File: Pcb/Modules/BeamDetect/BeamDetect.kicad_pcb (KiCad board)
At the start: 2 copper layers, 50.8 x 20.3 mm, 9 parts, among them J1 JACK_RJ45, U3 TSOP585xx, X1 HOLE, X2 HOLE, X3 HOLE, X4 HOLE

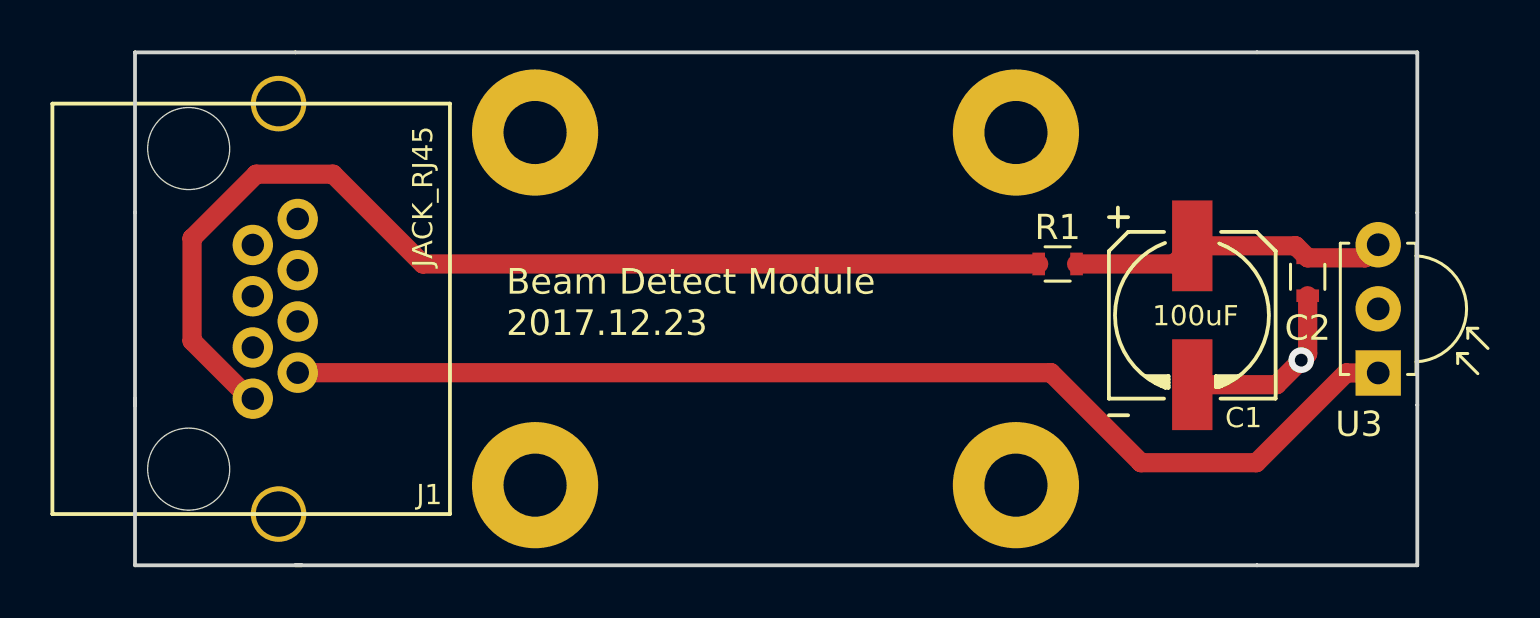
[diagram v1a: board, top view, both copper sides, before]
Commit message: Update module pcbs
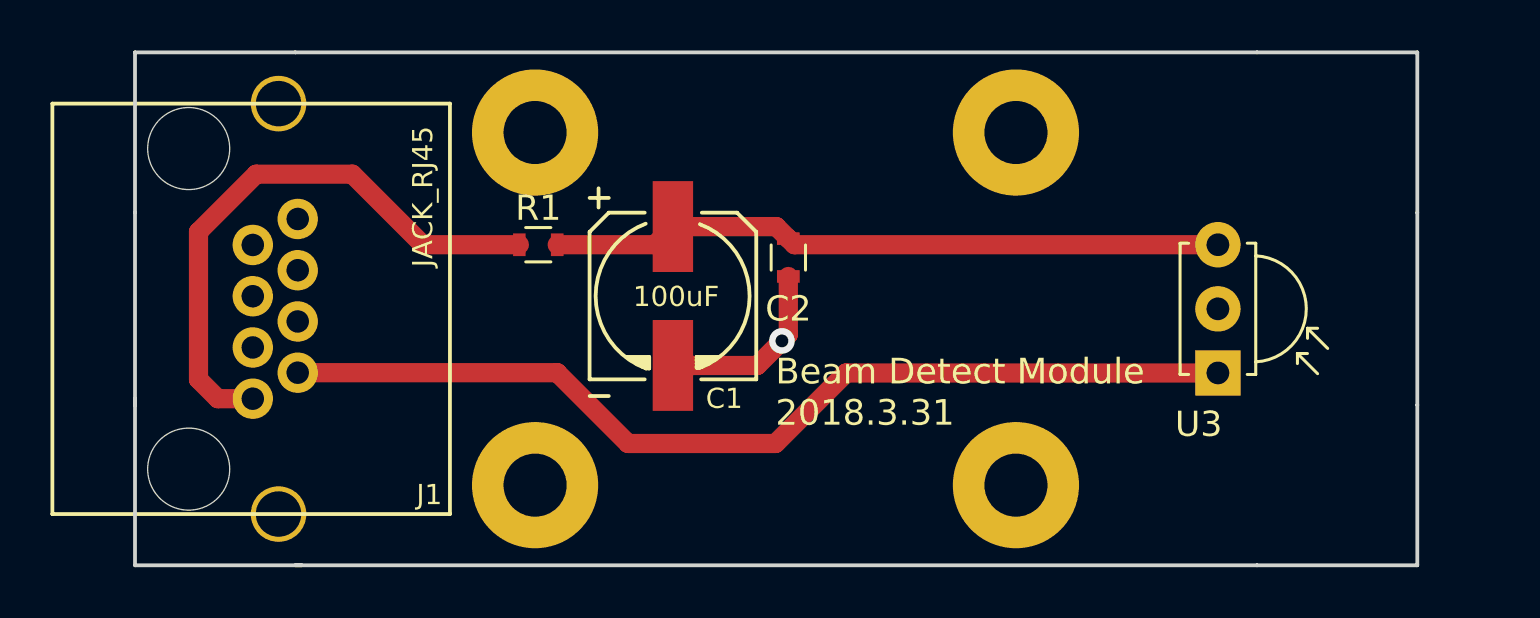
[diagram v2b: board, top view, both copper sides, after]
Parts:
- moved C1 20.6 mm to (56.9, 45.2)
- moved C2 20.6 mm to (61.5, 43.7)
- moved R1 20.6 mm to (51.6, 43.2)
- moved U3 6.35 mm to (78.5, 48.3)
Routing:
- net +3V3: track 43.9 -> 23.6 mm
- net Net-(C1-Pad1): track 12.7 -> 26.8 mm
- net Net-(J1-Pad2): track 46.0 -> 39.0 mm
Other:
- board text added: "Beam Detect Module 2018.3.31"
- board text removed: "Beam Detect Module 2017.12.23"
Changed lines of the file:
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@@
     (thickness 1.6)
     (drawings 13)
-    (tracks 25)
+    (tracks 26)
     (zones 0)
     (modules 9)
@@
   )
   (module Resistors_SMD:R_0603 (layer F.Cu)
-    (at 82.042 44.45 270)
+    (at 61.468 43.688 270)
     (descr "Resistor SMD 0603, reflow soldering, Vishay (see dcrcw.pdf)")
     (tags "resistor 0603")
@@
   )
   (module Opto-Devices:IRReceiver_Vishay_MINICAST-3pin (layer F.Cu)
-    (at 84.836 48.26 90)
+    (at 78.486 48.26 90)
     (descr "IR Receiver Vishay TSOP-xxxx, MINICAST package")
     (tags "IR Receiver Vishay TSOP-xxxx MINICAST")
@@
   )
   (module CA6:c_elec_6.3x5.7 (layer F.Cu)
-    (at 77.47 45.974 90)
+    (at 56.896 45.212 90)
     (descr "SMT capacitor, aluminium electrolytic, 6.3x5.7")
     (fp_text reference C1 (at -4.064 2.032 180) (layer F.SilkS)
@@
   )
   (module Resistors_SMD:R_0603 (layer F.Cu)
-    (at 72.136 43.942)
+    (at 51.562 43.18)
     (descr "Resistor SMD 0603, reflow soldering, Vishay (see dcrcw.pdf)")
     (tags "resistor 0603")
@@
   (gr_line (start 35.5854 41.91) (end 35.5854 49.53) (angle 90) (layer Edge.Cuts) (width 0.15))
   (gr_line (start 86.3854 41.91) (end 86.3854 49.53) (angle 90) (layer Edge.Cuts) (width 0.15))
-  (gr_text "Beam Detect Module\n2017.12.23" (at 50.292 45.466) (layer F.SilkS)
+  (gr_text "Beam Detect Module\n2018.3.31" (at 60.96 49.022) (layer F.SilkS)
     (effects (font (size 1.016 1.016) (thickness 0.2032)) (justify left))
   )
   (gr_line (start 80.0354 55.88) (end 41.9354 55.88) (angle 90) (layer Edge.Cuts) (width 0.15))
   (gr_line (start 41.9354 35.56) (end 80.0354 35.56) (angle 90) (layer Edge.Cuts) (width 0.15))
-  (segment (start 77.47 48.7248) (end 80.8152 48.7248) (width 0.762) (layer F.Cu) (net 1))
-  (segment (start 82.042 47.498) (end 81.788 47.752) (width 0.762) (layer F.Cu) (net 1))
-  (via (at 81.788 47.752) (size 1.016) (drill 0.508) (layers F.Cu B.Cu) (net 1))
-  (segment (start 82.042 47.498) (end 82.042 45.2) (width 0.762) (layer F.Cu) (net 1))
-  (segment (start 80.8152 48.7248) (end 81.788 47.752) (width 0.762) (layer F.Cu) (net 1))
-  (segment (start 42.032 48.25) (end 71.872 48.25) (width 0.762) (layer F.Cu) (net 2))
-  (segment (start 83.566 48.26) (end 84.836 48.26) (width 0.762) (layer F.Cu) (net 2))
-  (segment (start 80.01 51.816) (end 83.566 48.26) (width 0.762) (layer F.Cu) (net 2))
-  (segment (start 75.438 51.816) (end 80.01 51.816) (width 0.762) (layer F.Cu) (net 2))
-  (segment (start 71.872 48.25) (end 75.438 51.816) (width 0.762) (layer F.Cu) (net 2))
-  (segment (start 84.836 48.26) (end 84.582 48.26) (width 0.508) (layer F.Cu) (net 2))
+  (segment (start 56.896 47.9628) (end 60.2412 47.9628) (width 0.762) (layer F.Cu) (net 1))
+  (segment (start 61.468 46.736) (end 61.214 46.99) (width 0.762) (layer F.Cu) (net 1))
+  (via (at 61.214 46.99) (size 1.016) (drill 0.508) (layers F.Cu B.Cu) (net 1))
+  (segment (start 61.468 46.736) (end 61.468 44.438) (width 0.762) (layer F.Cu) (net 1))
+  (segment (start 60.2412 47.9628) (end 61.214 46.99) (width 0.762) (layer F.Cu) (net 1))
+  (segment (start 78.486 48.26) (end 63.754 48.26) (width 0.762) (layer F.Cu) (net 2) (status 10))
+  (segment (start 52.314 48.25) (end 42.032 48.25) (width 0.762) (layer F.Cu) (net 2))
+  (segment (start 55.118 51.054) (end 52.314 48.25) (width 0.762) (layer F.Cu) (net 2))
+  (segment (start 60.96 51.054) (end 55.118 51.054) (width 0.762) (layer F.Cu) (net 2))
+  (segment (start 63.754 48.26) (end 60.96 51.054) (width 0.762) (layer F.Cu) (net 2))
+  (segment (start 78.486 48.26) (end 78.232 48.26) (width 0.508) (layer F.Cu) (net 2) (status 30))
+  (segment (start 38.866 49.28) (end 40.252 49.28) (width 0.762) (layer F.Cu) (net 3))
+  (segment (start 38.1 48.514) (end 38.866 49.28) (width 0.762) (layer F.Cu) (net 3))
+  (segment (start 38.1 42.672) (end 38.1 48.514) (width 0.762) (layer F.Cu) (net 3))
+  (segment (start 40.386 40.386) (end 38.1 42.672) (width 0.762) (layer F.Cu) (net 3))
+  (segment (start 44.196 40.386) (end 40.386 40.386) (width 0.762) (layer F.Cu) (net 3))
+  (segment (start 46.99 43.18) (end 44.196 40.386) (width 0.762) (layer F.Cu) (net 3))
+  (segment (start 50.812 43.18) (end 46.99 43.18) (width 0.762) (layer F.Cu) (net 3))
   (segment (start 40.252 49.28) (end 40.136 49.28) (width 0.762) (layer F.Cu) (net 3))
-  (segment (start 40.136 49.28) (end 37.846 46.99) (width 0.762) (layer F.Cu) (net 3))
-  (segment (start 46.99 43.942) (end 71.386 43.942) (width 0.762) (layer F.Cu) (net 3))
-  (segment (start 43.434 40.386) (end 46.99 43.942) (width 0.762) (layer F.Cu) (net 3))
-  (segment (start 40.386 40.386) (end 43.434 40.386) (width 0.762) (layer F.Cu) (net 3))
-  (segment (start 37.846 42.926) (end 40.386 40.386) (width 0.762) (layer F.Cu) (net 3))
-  (segment (start 37.846 46.99) (end 37.846 42.926) (width 0.762) (layer F.Cu) (net 3))
   (segment (start 40.252 49.28) (end 40.644 49.28) (width 0.762) (layer F.Cu) (net 3))
-  (segment (start 82.042 43.7) (end 84.316 43.7) (width 0.762) (layer F.Cu) (net 4))
-  (segment (start 84.316 43.7) (end 84.836 43.18) (width 0.762) (layer F.Cu) (net 4))
-  (segment (start 77.47 43.2232) (end 81.5652 43.2232) (width 0.762) (layer F.Cu) (net 4))
-  (segment (start 81.5652 43.2232) (end 82.042 43.7) (width 0.762) (layer F.Cu) (net 4))
-  (segment (start 72.886 43.942) (end 76.7512 43.942) (width 0.762) (layer F.Cu) (net 4))
-  (segment (start 76.7512 43.942) (end 77.47 43.2232) (width 0.762) (layer F.Cu) (net 4))
+  (segment (start 78.486 43.18) (end 61.71 43.18) (width 0.762) (layer F.Cu) (net 4) (status 10))
+  (segment (start 61.71 43.18) (end 61.468 42.938) (width 0.762) (layer F.Cu) (net 4))
+  (segment (start 56.896 42.4612) (end 60.9912 42.4612) (width 0.762) (layer F.Cu) (net 4))
+  (segment (start 60.9912 42.4612) (end 61.468 42.938) (width 0.762) (layer F.Cu) (net 4))
+  (segment (start 52.312 43.18) (end 56.1772 43.18) (width 0.762) (layer F.Cu) (net 4))
+  (segment (start 56.1772 43.18) (end 56.896 42.4612) (width 0.762) (layer F.Cu) (net 4))
   (zone (net 1) (net_name GND) (layer B.Cu) (hatch edge 0.508)
     (connect_pads (clearance 0.508))

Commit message: Update pcbs
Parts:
- moved U3 5.71 mm to (84.2, 48.3)
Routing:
- net Net-(C1-Pad1): track 26.8 -> 32.5 mm
- net Net-(J1-Pad2): track 39.0 -> 44.7 mm
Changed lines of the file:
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@@
     (links 10)
     (no_connects 0)
-    (area 31.983069 34.206 89.500001 57.334)
+    (area 31.983069 34.206 86.460401 57.334)
     (thickness 1.6)
     (drawings 13)
@@
   )
   (module Opto-Devices:IRReceiver_Vishay_MINICAST-3pin (layer F.Cu)
-    (at 78.486 48.26 90)
+    (at 84.201 48.26 90)
     (descr "IR Receiver Vishay TSOP-xxxx, MINICAST package")
     (tags "IR Receiver Vishay TSOP-xxxx MINICAST")
@@
   (gr_line (start 35.5854 41.91) (end 35.5854 49.53) (angle 90) (layer Edge.Cuts) (width 0.15))
   (gr_line (start 86.3854 41.91) (end 86.3854 49.53) (angle 90) (layer Edge.Cuts) (width 0.15))
-  (gr_text "Beam Detect Module\n2018.3.31" (at 60.96 49.022) (layer F.SilkS)
+  (gr_text "Beam Detect Module\n2018.3.31" (at 64.77 46.101) (layer F.SilkS)
     (effects (font (size 1.016 1.016) (thickness 0.2032)) (justify left))
   )
   (gr_line (start 80.0354 55.88) (end 41.9354 55.88) (angle 90) (layer Edge.Cuts) (width 0.15))
   (gr_line (start 41.9354 35.56) (end 80.0354 35.56) (angle 90) (layer Edge.Cuts) (width 0.15))
-  (segment (start 56.896 47.9628) (end 60.2412 47.9628) (width 0.762) (layer F.Cu) (net 1))
+  (segment (start 56.896 47.9628) (end 60.2412 47.9628) (width 0.762) (layer F.Cu) (net 1) (status 10))
   (segment (start 61.468 46.736) (end 61.214 46.99) (width 0.762) (layer F.Cu) (net 1))
   (via (at 61.214 46.99) (size 1.016) (drill 0.508) (layers F.Cu B.Cu) (net 1))
-  (segment (start 61.468 46.736) (end 61.468 44.438) (width 0.762) (layer F.Cu) (net 1))
+  (segment (start 61.468 46.736) (end 61.468 44.438) (width 0.762) (layer F.Cu) (net 1) (status 20))
   (segment (start 60.2412 47.9628) (end 61.214 46.99) (width 0.762) (layer F.Cu) (net 1))
-  (segment (start 78.486 48.26) (end 63.754 48.26) (width 0.762) (layer F.Cu) (net 2) (status 10))
-  (segment (start 52.314 48.25) (end 42.032 48.25) (width 0.762) (layer F.Cu) (net 2))
+  (segment (start 84.201 48.26) (end 63.754 48.26) (width 0.762) (layer F.Cu) (net 2) (status 10))
+  (segment (start 52.314 48.25) (end 42.032 48.25) (width 0.762) (layer F.Cu) (net 2) (status 20))
   (segment (start 55.118 51.054) (end 52.314 48.25) (width 0.762) (layer F.Cu) (net 2))
   (segment (start 60.96 51.054) (end 55.118 51.054) (width 0.762) (layer F.Cu) (net 2))
   (segment (start 63.754 48.26) (end 60.96 51.054) (width 0.762) (layer F.Cu) (net 2))
-  (segment (start 78.486 48.26) (end 78.232 48.26) (width 0.508) (layer F.Cu) (net 2) (status 30))
-  (segment (start 38.866 49.28) (end 40.252 49.28) (width 0.762) (layer F.Cu) (net 3))
+  (segment (start 84.201 48.26) (end 83.947 48.26) (width 0.508) (layer F.Cu) (net 2) (status 30))
+  (segment (start 38.866 49.28) (end 40.252 49.28) (width 0.762) (layer F.Cu) (net 3) (status 20))
   (segment (start 38.1 48.514) (end 38.866 49.28) (width 0.762) (layer F.Cu) (net 3))
   (segment (start 38.1 42.672) (end 38.1 48.514) (width 0.762) (layer F.Cu) (net 3))
@@
   (segment (start 44.196 40.386) (end 40.386 40.386) (width 0.762) (layer F.Cu) (net 3))
   (segment (start 46.99 43.18) (end 44.196 40.386) (width 0.762) (layer F.Cu) (net 3))
-  (segment (start 50.812 43.18) (end 46.99 43.18) (width 0.762) (layer F.Cu) (net 3))
-  (segment (start 40.252 49.28) (end 40.136 49.28) (width 0.762) (layer F.Cu) (net 3))
-  (segment (start 40.252 49.28) (end 40.644 49.28) (width 0.762) (layer F.Cu) (net 3))
-  (segment (start 78.486 43.18) (end 61.71 43.18) (width 0.762) (layer F.Cu) (net 4) (status 10))
-  (segment (start 61.71 43.18) (end 61.468 42.938) (width 0.762) (layer F.Cu) (net 4))
-  (segment (start 56.896 42.4612) (end 60.9912 42.4612) (width 0.762) (layer F.Cu) (net 4))
-  (segment (start 60.9912 42.4612) (end 61.468 42.938) (width 0.762) (layer F.Cu) (net 4))
-  (segment (start 52.312 43.18) (end 56.1772 43.18) (width 0.762) (layer F.Cu) (net 4))
-  (segment (start 56.1772 43.18) (end 56.896 42.4612) (width 0.762) (layer F.Cu) (net 4))
+  (segment (start 50.812 43.18) (end 46.99 43.18) (width 0.762) (layer F.Cu) (net 3) (status 10))
+  (segment (start 40.252 49.28) (end 40.136 49.28) (width 0.762) (layer F.Cu) (net 3) (status 30))
+  (segment (start 40.252 49.28) (end 40.644 49.28) (width 0.762) (layer F.Cu) (net 3) (status 30))
+  (segment (start 84.201 43.18) (end 61.71 43.18) (width 0.762) (layer F.Cu) (net 4) (status 30))
+  (segment (start 61.71 43.18) (end 61.468 42.938) (width 0.762) (layer F.Cu) (net 4) (status 30))
+  (segment (start 56.896 42.4612) (end 60.9912 42.4612) (width 0.762) (layer F.Cu) (net 4) (status 10))
+  (segment (start 60.9912 42.4612) (end 61.468 42.938) (width 0.762) (layer F.Cu) (net 4) (status 20))
+  (segment (start 52.312 43.18) (end 56.1772 43.18) (width 0.762) (layer F.Cu) (net 4) (status 30))
+  (segment (start 56.1772 43.18) (end 56.896 42.4612) (width 0.762) (layer F.Cu) (net 4) (status 30))
   (zone (net 1) (net_name GND) (layer B.Cu) (hatch edge 0.508)
     (connect_pads (clearance 0.508))

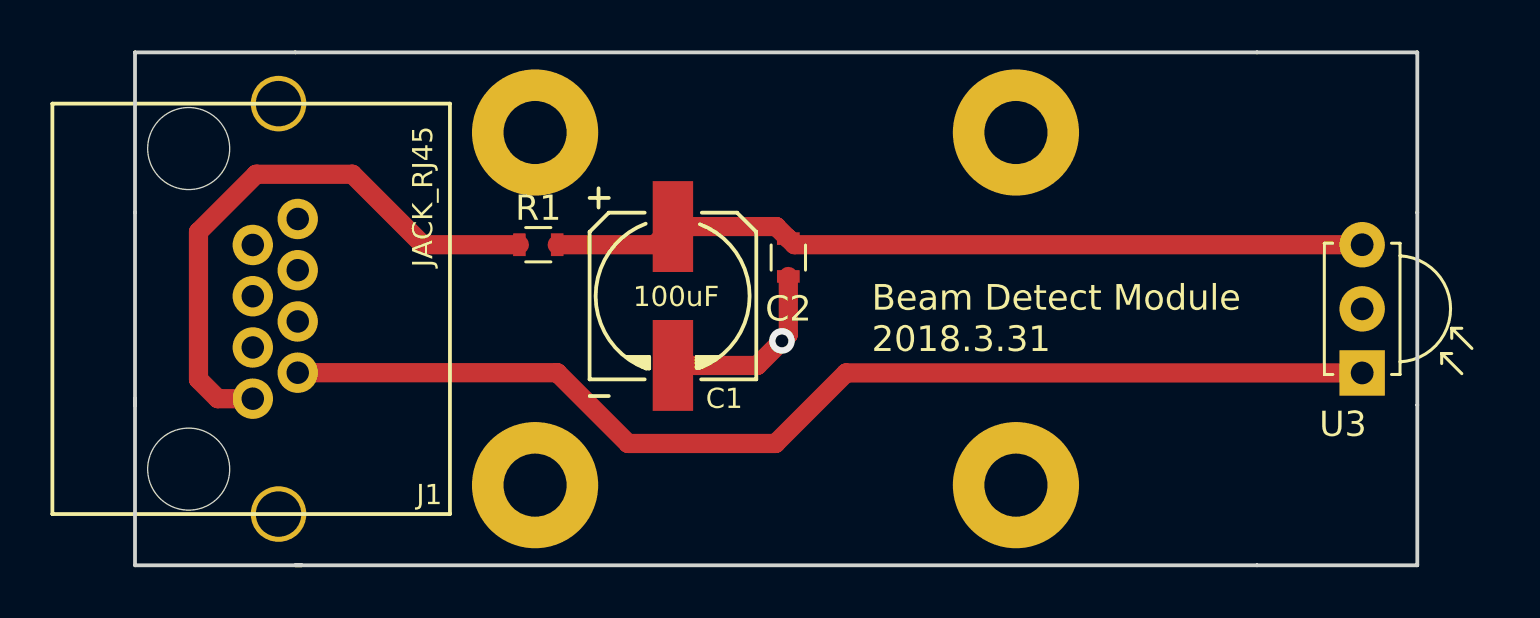
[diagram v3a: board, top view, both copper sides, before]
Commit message: Update module pcbs to fix minor issues and round corners
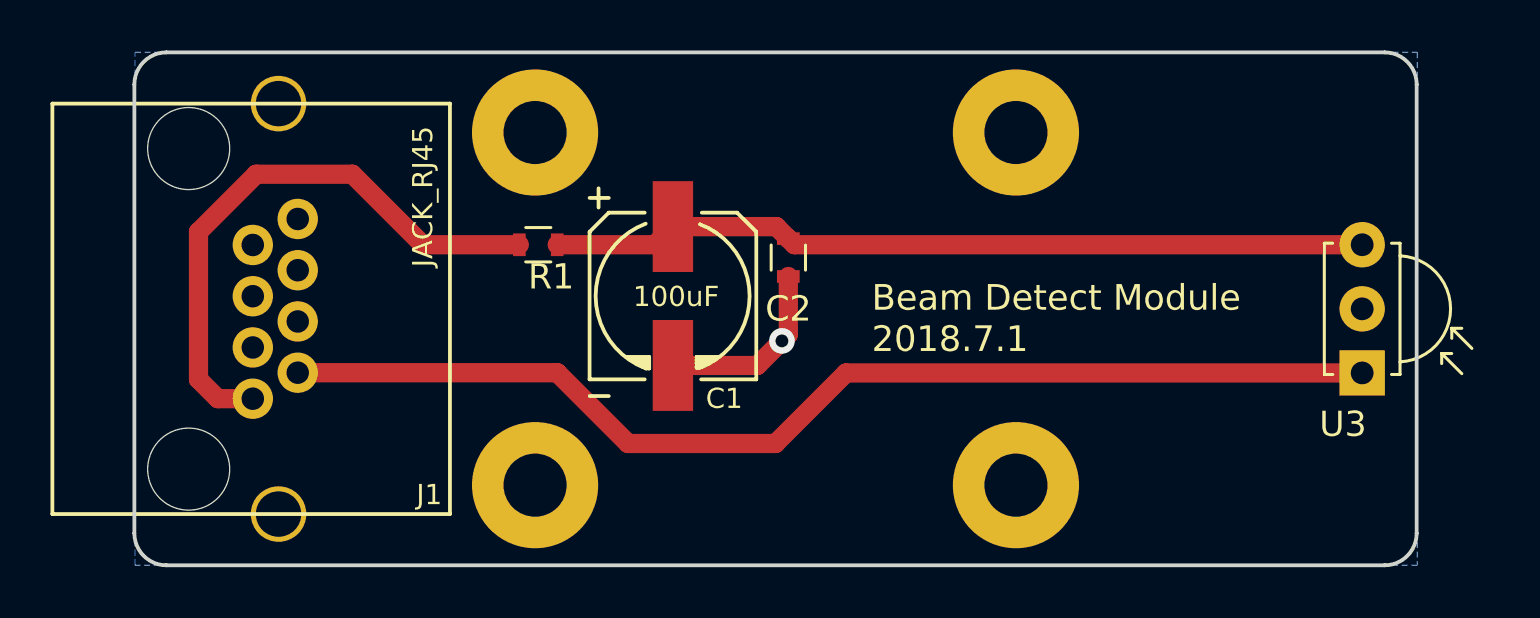
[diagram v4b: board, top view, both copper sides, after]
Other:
- outline, holes or cut-outs redrawn
- board text added: "Beam Detect Module 2018.7.1"
- board text removed: "Beam Detect Module 2018.3.31"
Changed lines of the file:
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@@
     (links 10)
     (no_connects 0)
-    (area 31.983069 34.206 86.460401 57.334)
+    (area 31.983069 34.206 88.865001 57.334)
     (thickness 1.6)
-    (drawings 13)
+    (drawings 9)
     (tracks 26)
     (zones 0)
@@
     (tags "resistor 0603")
     (attr smd)
-    (fp_text reference R1 (at 0 -1.45) (layer F.SilkS)
+    (fp_text reference R1 (at 0.508 1.27) (layer F.SilkS)
       (effects (font (size 1 1) (thickness 0.15)))
     )
@@
     (pad 1 thru_hole circle (at 0 0) (size 5 5) (drill 2.5) (layers *.Cu *.Mask))
   )
-  (gr_line (start 86.3854 35.56) (end 86.3854 41.91) (angle 90) (layer Edge.Cuts) (width 0.15))
-  (gr_line (start 80.0354 35.56) (end 86.3854 35.56) (angle 90) (layer Edge.Cuts) (width 0.15))
-  (gr_line (start 86.3854 55.88) (end 80.0354 55.88) (angle 90) (layer Edge.Cuts) (width 0.15))
-  (gr_line (start 86.3854 49.53) (end 86.3854 55.88) (angle 90) (layer Edge.Cuts) (width 0.15))
-  (gr_line (start 35.5854 35.56) (end 35.5854 41.91) (angle 90) (layer Edge.Cuts) (width 0.15))
-  (gr_line (start 41.9354 35.56) (end 35.5854 35.56) (angle 90) (layer Edge.Cuts) (width 0.15))
-  (gr_line (start 35.5854 55.88) (end 35.5854 49.276) (angle 90) (layer Edge.Cuts) (width 0.15))
-  (gr_line (start 42.1894 55.88) (end 35.5854 55.88) (angle 90) (layer Edge.Cuts) (width 0.15))
-  (gr_line (start 35.5854 41.91) (end 35.5854 49.53) (angle 90) (layer Edge.Cuts) (width 0.15))
-  (gr_line (start 86.3854 41.91) (end 86.3854 49.53) (angle 90) (layer Edge.Cuts) (width 0.15))
-  (gr_text "Beam Detect Module\n2018.3.31" (at 64.77 46.101) (layer F.SilkS)
+  (gr_line (start 86.36 36.83) (end 86.36 54.61) (angle 90) (layer Edge.Cuts) (width 0.15))
+  (gr_line (start 36.83 35.56) (end 85.09 35.56) (angle 90) (layer Edge.Cuts) (width 0.15))
+  (gr_line (start 35.56 54.61) (end 35.56 36.83) (angle 90) (layer Edge.Cuts) (width 0.15))
+  (gr_line (start 85.09 55.88) (end 36.83 55.88) (angle 90) (layer Edge.Cuts) (width 0.15))
+  (gr_arc (start 36.83 54.61) (end 36.83 55.88) (angle 90) (layer Edge.Cuts) (width 0.15))
+  (gr_arc (start 85.09 54.61) (end 86.36 54.61) (angle 90) (layer Edge.Cuts) (width 0.15))
+  (gr_arc (start 36.83 36.83) (end 35.56 36.83) (angle 90) (layer Edge.Cuts) (width 0.15))
+  (gr_arc (start 85.09 36.83) (end 85.09 35.56) (angle 90) (layer Edge.Cuts) (width 0.15))
+  (gr_text "Beam Detect Module\n2018.7.1" (at 64.77 46.101) (layer F.SilkS)
     (effects (font (size 1.016 1.016) (thickness 0.2032)) (justify left))
   )
-  (gr_line (start 80.0354 55.88) (end 41.9354 55.88) (angle 90) (layer Edge.Cuts) (width 0.15))
-  (gr_line (start 41.9354 35.56) (end 80.0354 35.56) (angle 90) (layer Edge.Cuts) (width 0.15))
   (segment (start 56.896 47.9628) (end 60.2412 47.9628) (width 0.762) (layer F.Cu) (net 1) (status 10))
   (segment (start 61.468 46.736) (end 61.214 46.99) (width 0.762) (layer F.Cu) (net 1))
